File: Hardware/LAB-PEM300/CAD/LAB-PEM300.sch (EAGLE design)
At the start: 4 parts, among them IC1 AD7992, IC2 TPS77028

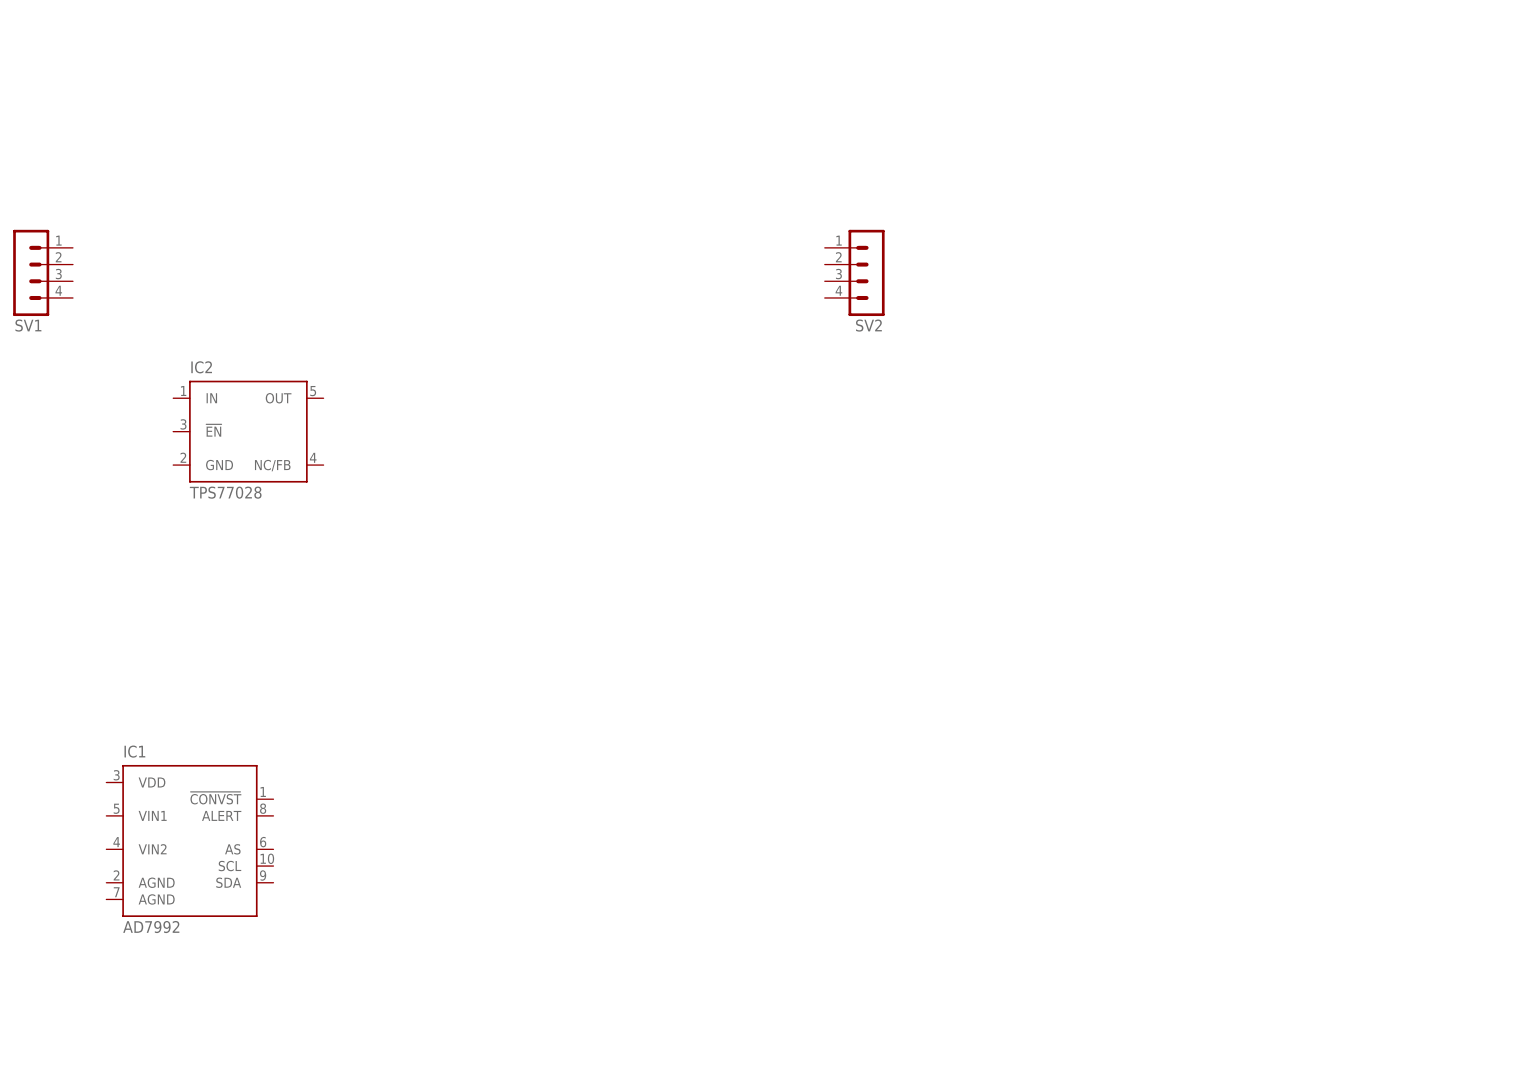
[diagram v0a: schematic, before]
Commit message: Completed LAB-PEM300 Design, Layout, BOM
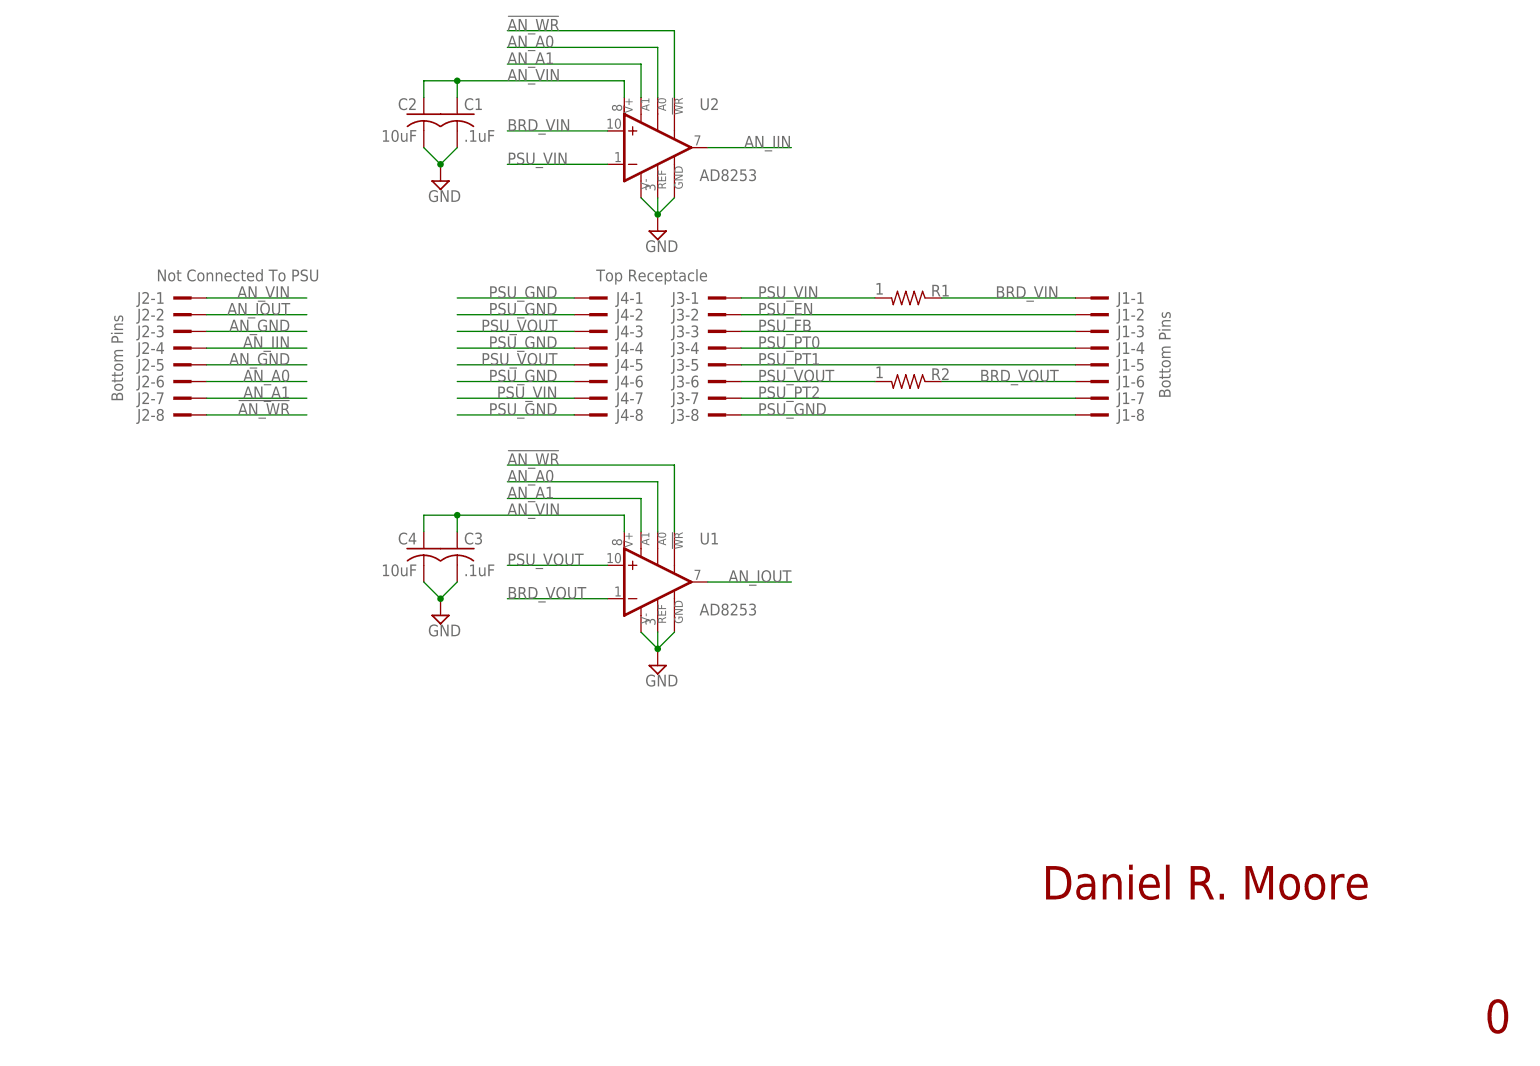
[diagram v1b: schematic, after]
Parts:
- removed IC1: AD7992, analog-devices:AD7992
- removed IC2: TPS77028, texas:TPS77028
- removed SV1, SV2: (no value), con-lstb:MA04-1
- added C1, C3: .1uF, rcl:C-USC0402
- added C2, C4: 10uF, rcl:C-USC0402
- added J1, J2: SULLINSSMTPINHEADER-8, LAB-PEM300:SULLINSSMTPINHEADER-8
- added J3, J4: (no value), LAB-PEM300:MILLMAXSMTFEMALE-8
- added R1, R2: 1, rcl:R-US_R2512
- added U1, U2: AD8253, LAB-PEM300:AD8253
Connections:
- new net !AN_WR: J2-8.KL, U1.!WR, U2.!WR
- new net AN_A0: J2-6.KL, U1.A0, U2.A0
- new net AN_A1: J2-7.KL, U1.A1, U2.A1
- new net AN_GND: C1.2, C2.2, C3.2, C4.2, J2-3.KL, J2-5.KL, U1.DGND, U1.REF, U1.V-, U2.DGND, U2.REF, U2.V-
- new net AN_IIN: J2-4.KL, U2.OUT
- new net AN_IOUT: J2-2.KL, U1.OUT
- new net AN_VIN: C1.1, C2.1, C3.1, C4.1, J2-1.KL, U1.V+, U2.V+
- new net BRD_VIN: J1-1.KL, R1.1, U2.+IN
- new net BRD_VOUT: J1-6.KL, R2.1, U1.-IN
- new net PSU_EN: J1-2.KL, J3-2.KL
- new net PSU_FB: J1-3.KL, J3-3.KL
- new net PSU_GND: J1-8.KL, J3-8.KL, J4-1.KL, J4-2.KL, J4-4.KL, J4-6.KL, J4-8.KL
- new net PSU_PT0: J1-4.KL, J3-4.KL
- new net PSU_PT1: J1-5.KL, J3-5.KL
- new net PSU_PT2: J1-7.KL, J3-7.KL
- new net PSU_VIN: J3-1.KL, J4-7.KL, R1.2, U2.-IN
- new net PSU_VOUT: J3-6.KL, J4-3.KL, J4-5.KL, R2.2, U1.+IN
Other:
- note added: "0"
- note added: "Bottom Pins"
- note added: "Daniel R. Moore"
- note added: "Not Connected To PSU"
- note added: "Top Receptacle"
